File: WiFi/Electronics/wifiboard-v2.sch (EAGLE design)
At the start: 16 parts, among them IC2 7805DT, Q1 FDD8870, X1 MKDSN1,5/2-5,08, X2 MKDSN1,5/2-5,08

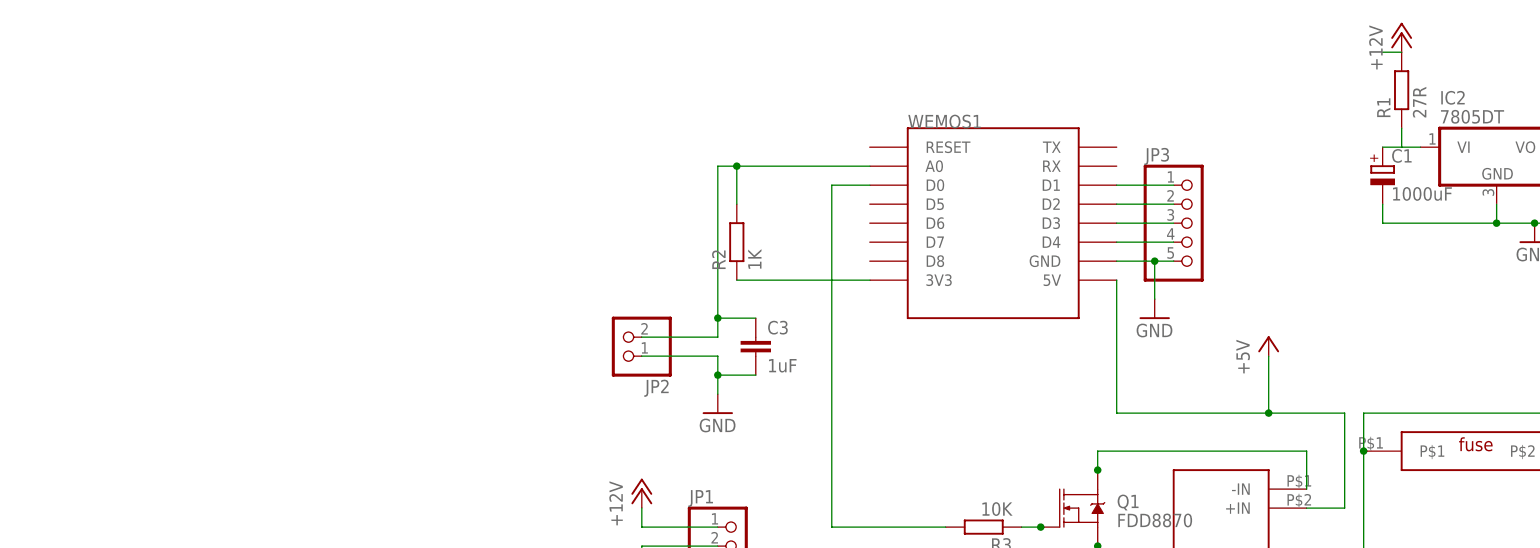
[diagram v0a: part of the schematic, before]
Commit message: heating.php improved to check that times monotonically increase throughout the day.
Various bits of experimental WiFi electronics added.
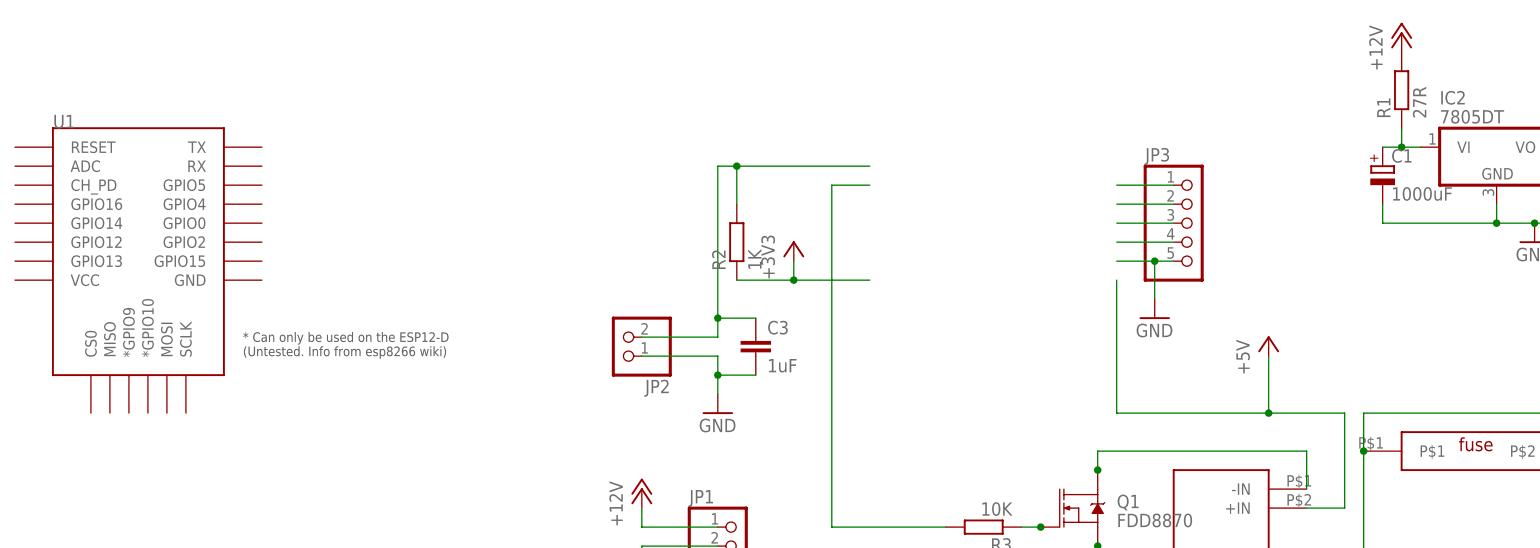
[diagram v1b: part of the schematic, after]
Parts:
- removed WEMOS1: (no value), esp8266modules:WEMOS-D1-MINI
- added U1: (no value), esp8266modules:ESP12ESMD
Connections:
- removed net N$11: JP3.4, WEMOS1.D4
- removed net N$13: JP3.3, WEMOS1.D3
- removed net N$14: JP3.2, WEMOS1.D2
- removed net N$15: JP3.1, WEMOS1.D1
- removed net N$3: C3.1, JP2.2, R2.2, WEMOS1.A0
- removed net N$4: R2.1, WEMOS1.3V3
- removed net N$6: R3.2, WEMOS1.D0
- new net +3V3: R2.1
- new net A0: C3.1, JP2.2, R2.2
- new net D0: R3.2
- new net D1: JP3.1
- new net D2: JP3.2
- new net D3: JP3.3
- new net D4: JP3.4
- net +5V: no longer WEMOS1.5V
- net GND: no longer WEMOS1.GND
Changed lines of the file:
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@@
 </classes>
 <parts>
-<part name="WEMOS1" library="esp8266modules" deviceset="WEMOS-D1-MINI" device=""/>
 <part name="GND1" library="supply1" deviceset="GND" device=""/>
 <part name="P+1" library="supply1" deviceset="+12V" device=""/>
@@
 <part name="Q1" library="SparkFun-DiscreteSemi" deviceset="MOSFET-NCH" device="-FDD8780" value="FDD8870"/>
 <part name="C1" library="rcl" deviceset="CPOL-EU" device="B45181B" value="1000uF"/>
+<part name="U1" library="esp8266modules" deviceset="ESP12E" device="SMD"/>
+<part name="+3V1" library="supply1" deviceset="+3V3" device=""/>
 </parts>
 <sheets>
@@
 </plain>
 <instances>
-<instance part="WEMOS1" gate="D1" x="7.62" y="58.42"/>
 <instance part="GND1" gate="1" x="81.28" y="55.88"/>
 <instance part="P+1" gate="1" x="63.5" y="83.82"/>
@@
 <instance part="Q1" gate="NMOS" x="20.32" y="20.32"/>
 <instance part="C1" gate="G$1" x="60.96" y="66.04"/>
+<instance part="U1" gate="G$1" x="-104.14" y="60.96"/>
+<instance part="+3V1" gate="G$1" x="-17.78" y="55.88"/>
 </instances>
 <busses>
@@
 </segment>
 <segment>
-<pinref part="WEMOS1" gate="D1" pin="GND"/>
 <pinref part="JP3" gate="A" pin="5"/>
 <wire x1="25.4" y1="53.34" x2="30.48" y2="53.34" width="0.1524" layer="91"/>
@@
 <pinref part="R1" gate="G$1" pin="2"/>
 <pinref part="P+1" gate="1" pin="+12V"/>
-<wire x1="63.5" y1="81.28" x2="60.96" y2="81.28" width="0.1524" layer="91"/>
 </segment>
 <segment>
@@
 </segment>
 </net>
-<net name="N$3" class="0">
+<net name="A0" class="0">
 <segment>
 <pinref part="JP2" gate="G$1" pin="2"/>
 <wire x1="-38.1" y1="43.18" x2="-27.94" y2="43.18" width="0.1524" layer="91"/>
 <wire x1="-27.94" y1="43.18" x2="-27.94" y2="45.72" width="0.1524" layer="91"/>
-<pinref part="WEMOS1" gate="D1" pin="A0"/>
 <wire x1="-27.94" y1="45.72" x2="-27.94" y2="66.04" width="0.1524" layer="91"/>
 <wire x1="-27.94" y1="66.04" x2="-25.4" y2="66.04" width="0.1524" layer="91"/>
@@
 </segment>
 </net>
-<net name="N$4" class="0">
-<segment>
-<pinref part="WEMOS1" gate="D1" pin="3V3"/>
-<pinref part="R2" gate="G$1" pin="1"/>
-<wire x1="-7.62" y1="50.8" x2="-25.4" y2="50.8" width="0.1524" layer="91"/>
-</segment>
-</net>
 <net name="N$5" class="0">
 <segment>
@@
 </segment>
 </net>
-<net name="N$6" class="0">
-<segment>
-<pinref part="WEMOS1" gate="D1" pin="D0"/>
+<net name="D0" class="0">
+<segment>
 <wire x1="-7.62" y1="63.5" x2="-12.7" y2="63.5" width="0.1524" layer="91"/>
 <wire x1="-12.7" y1="63.5" x2="-12.7" y2="17.78" width="0.1524" layer="91"/>
@@
 </segment>
 </net>
-<net name="N$11" class="0">
+<net name="D4" class="0">
 <segment>
 <pinref part="JP3" gate="A" pin="4"/>
-<pinref part="WEMOS1" gate="D1" pin="D4"/>
 <wire x1="33.02" y1="55.88" x2="25.4" y2="55.88" width="0.1524" layer="91"/>
 </segment>
 </net>
-<net name="N$13" class="0">
+<net name="D3" class="0">
 <segment>
 <pinref part="JP3" gate="A" pin="3"/>
-<pinref part="WEMOS1" gate="D1" pin="D3"/>
 <wire x1="33.02" y1="58.42" x2="25.4" y2="58.42" width="0.1524" layer="91"/>
 </segment>
 </net>
-<net name="N$14" class="0">
+<net name="D2" class="0">
 <segment>
 <pinref part="JP3" gate="A" pin="2"/>
-<pinref part="WEMOS1" gate="D1" pin="D2"/>
 <wire x1="33.02" y1="60.96" x2="25.4" y2="60.96" width="0.1524" layer="91"/>
 </segment>
 </net>
-<net name="N$15" class="0">
+<net name="D1" class="0">
 <segment>
 <pinref part="JP3" gate="A" pin="1"/>
-<pinref part="WEMOS1" gate="D1" pin="D1"/>
 <wire x1="33.02" y1="63.5" x2="25.4" y2="63.5" width="0.1524" layer="91"/>
 </segment>
@@
 <wire x1="50.8" y1="20.32" x2="55.88" y2="20.32" width="0.1524" layer="91"/>
 <wire x1="55.88" y1="20.32" x2="55.88" y2="33.02" width="0.1524" layer="91"/>
-<pinref part="WEMOS1" gate="D1" pin="5V"/>
 <wire x1="55.88" y1="33.02" x2="45.72" y2="33.02" width="0.1524" layer="91"/>
 <wire x1="45.72" y1="33.02" x2="25.4" y2="33.02" width="0.1524" layer="91"/>
@@
 <pinref part="C1" gate="G$1" pin="+"/>
 <wire x1="63.5" y1="68.58" x2="60.96" y2="68.58" width="0.1524" layer="91"/>
-</segment>
-</net>
+<junction x="63.5" y="68.58"/>
+</segment>
+</net>
+<net name="+3V3" class="0">
+<segment>
+<pinref part="R2" gate="G$1" pin="1"/>
+<wire x1="-7.62" y1="50.8" x2="-17.78" y2="50.8" width="0.1524" layer="91"/>
+<pinref part="+3V1" gate="G$1" pin="+3V3"/>
+<wire x1="-17.78" y1="50.8" x2="-25.4" y2="50.8" width="0.1524" layer="91"/>
+<wire x1="-17.78" y1="53.34" x2="-17.78" y2="50.8" width="0.1524" layer="91"/>
+<junction x="-17.78" y="50.8"/>
+</segment>
+</net>

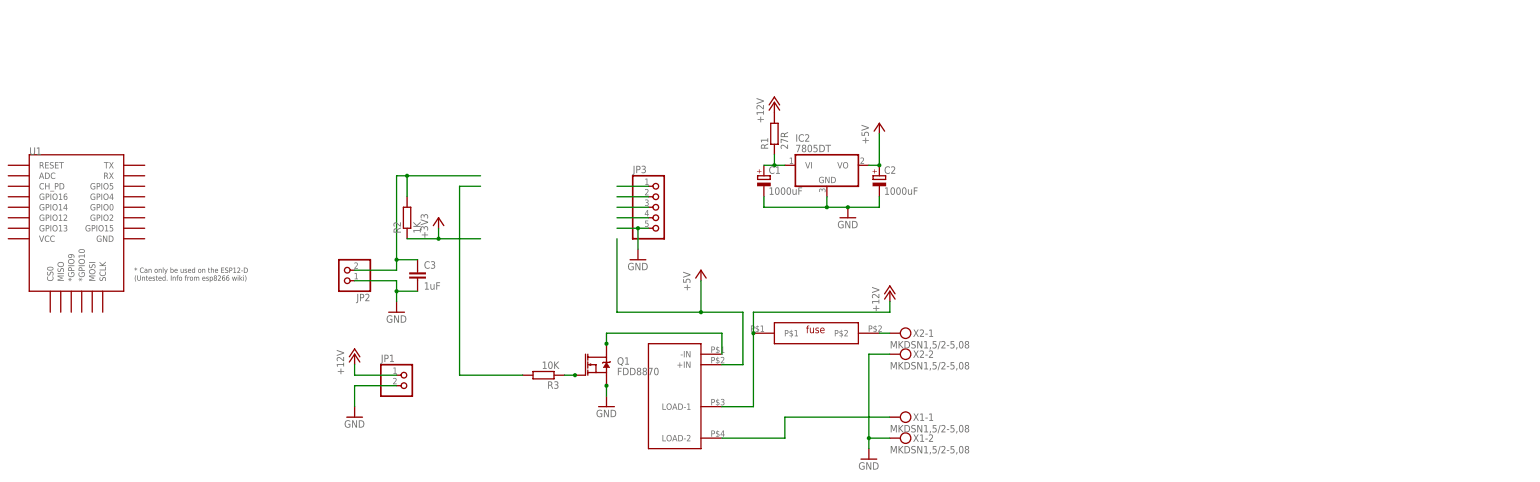
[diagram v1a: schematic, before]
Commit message: Simple web monitoring added to the thermostat program.
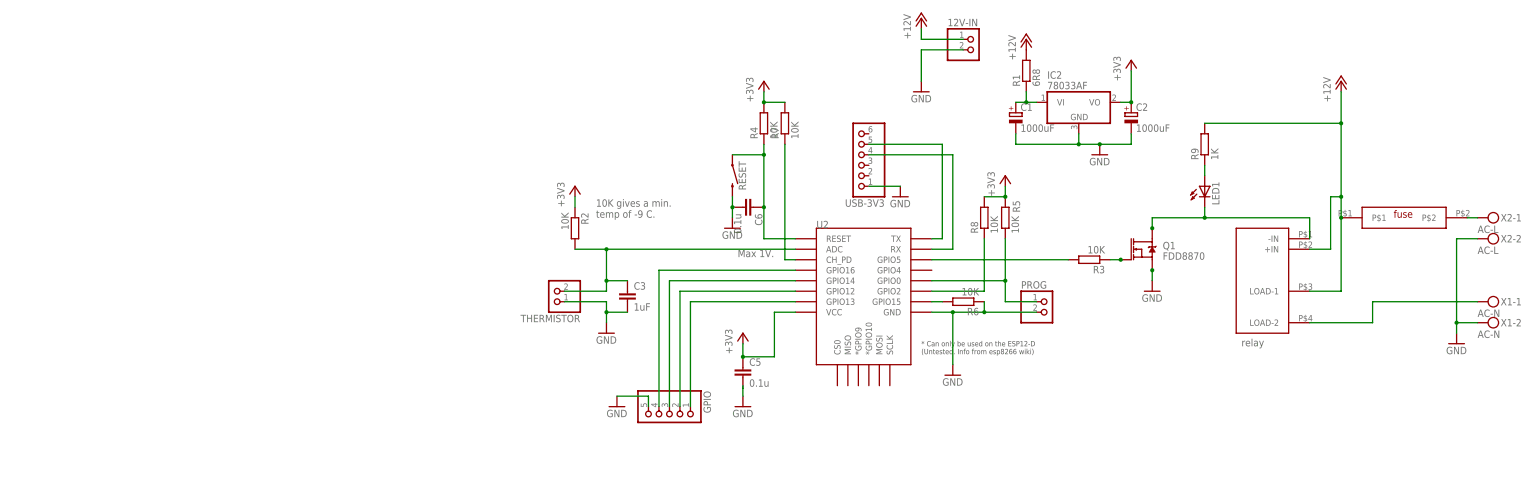
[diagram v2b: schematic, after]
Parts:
- removed JP1, JP2: (no value), pinhead:PINHD-1X2
- removed JP3: (no value), pinhead:PINHD-1X5
- removed U$1: OMRON-G6DS, alexa:OMRON-G6DS
- removed U$2: FUSE, alexa:FUSE
- removed U1: (no value), esp8266modules:ESP12ESMD
- added 12V-IN, PROG, THERMISTOR: (no value), pinhead:PINHD-1X2
- added C5, C6: 0.1u, rcl:C-EUC0805
- added FUSE: FUSE, alexa:FUSE
- added GPIO: (no value), pinhead:PINHD-1X5
- added LED1: (no value), led:LED3MM
- added R4, R5, R6, R7, R8: 10K, rcl:R-EU_R0805
- added R9: 1K, rcl:R-EU_R0805
- added RELAY: OMRON-G6DS, alexa:OMRON-G6DS
- added RESET: (no value), SparkFun-Switches:MOMENTARY-SWITCH-SPST-SMD-4.6X2.8MM
- added U2: (no value), esp8266modules:ESP12ESMD
- added USB-3V3: (no value), pinhead:PINHD-1X6
- IC2: value 7805DT -> 78033AF
- R1: value 27R -> 6R8
- R2: value 1K -> 10K
- X1: value MKDSN1,5/2-5,08 -> AC-N
- X2: value MKDSN1,5/2-5,08 -> AC-L
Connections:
- removed net +5V: C2.+, IC2.VO, U$1.+IN
- removed net D0: R3.2
- removed net D1: JP3.1
- removed net D2: JP3.2
- removed net D3: JP3.3
- removed net D4: JP3.4
- new net 0: PROG.1, R5.1, U2.GPIO0
- new net 12: GPIO.2, U2.GPIO12
- new net 13: GPIO.1, U2.GPIO13
- new net 14: GPIO.3, U2.GPIO14
- new net 15: R6.2, U2.GPIO15
- new net 16: GPIO.4, U2.GPIO16
- new net 2: R8.1, U2.GPIO2
- new net 5: R3.2, U2.GPIO5
- new net CH_PD: R7.1, U2.CH_PD
- new net N$14: LED1.A, R9.1
- new net RST: C6.1, R4.1, RESET.1, U2.RESET
- new net RX: U2.RX, USB-3V3.4
- new net TX: U2.TX, USB-3V3.5
- net +12V: now also 12V-IN.1, FUSE.P$1, R9.2, RELAY.+IN, RELAY.LOAD-1; no longer JP1.1, U$1.LOAD-1, U$2.P$1
- net +3V3: now also C2.+, C5.1, IC2.VO, R4.2, R5.2, R7.2, R8.2, U2.VCC
- net A0: now also THERMISTOR.2, U2.ADC; no longer JP2.2
- net GND: now also 12V-IN.2, C5.2, C6.2, GPIO.5, PROG.2, R6.1, RESET.2, THERMISTOR.1, U2.GND, USB-3V3.1; no longer JP1.2, JP2.1, JP3.5
- net N$10: now also RELAY.LOAD-2; no longer U$1.LOAD-2
- net N$12: now also FUSE.P$2; no longer U$2.P$2
- net N$7: now also LED1.C, RELAY.-IN; no longer U$1.-IN
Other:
- note added: "10K gives a min. temp of -9 C."
- note added: "Max 1V."
- note added: "relay"
- moved on the sheet: C1, C2, C3, IC2, Q1, R1, R2, R3, X1-1, X1-2, X2-1, X2-2
